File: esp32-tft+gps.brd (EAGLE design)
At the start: 34.2 x 64.8 mm, 36 parts, among them IC1 TCAN1051HGV, J4 Vertical Qwiic Connector, U2 XN04312, U8 NCP1117LPST50T3G

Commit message: actually save
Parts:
- removed -_+_G_V_T_R_E_0, -_+_G_V_T_R_E_1: MF-CON-2.54mm-01x08, SparkFun-Connectors:1X08
- removed C_SER, POW12, POW5: (no value), MF_Passives:C0603
- removed D2: BAS16, SparkFun-DiscreteSemi:SOD-323
- removed IC1: TCAN1051HGV, microbuilder:SOIC8_150MIL
- removed JP1: DB9, SparkFun-Connectors:DB9
- removed R1, R3, RCAN: (no value), 00jim:R0603
- removed U2: XN04312, SparkFun-DiscreteSemi:SOT23-6
- removed U3: (no value), SparkFun-IC-Power:TO220-IGO
- added J5: (no value), SparkFun-Connectors:1X02
- moved U$1 23.8 mm to (10.4, 25.4), turned to 0 degrees
- moved U$2 22.7 mm to (17.3, 25.4), turned to 180 degrees
- moved RCAN2 22.7 mm to (31.5, 38.6), turned to 90 degrees
- moved J2 20.8 mm to (2.03, 11.2)
- moved RCAN1 20.3 mm to (29.2, 38.6), turned to 90 degrees
- moved J1 16.8 mm to (4.06, 31.0)
- moved CEN 13.7 mm to (18.0, 31.8)
- moved R2 13.7 mm to (13.0, 36.1)
- moved R9 13.7 mm to (13.0, 31.8)
- moved REN 13.7 mm to (15.5, 31.8)
- moved RGP00 13.7 mm to (15.5, 36.1)
- moved TT1 13.7 mm to (9.40, 36.1)
- moved TT2 13.7 mm to (9.40, 31.8)
- moved J4 8.20 mm to (23.9, 39.4), turned to 180 degrees
- moved D1 5.95 mm to (12.7, 28.4)
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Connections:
- removed net CAN_H: IC1.7, JP1.1, RCAN.P$2
- removed net CAN_L: IC1.6, JP1.2, RCAN.P$1
- removed net N$4: C_SER.P$1, D2.A, R3.P$1
- removed net RAW: -_+_G_V_T_R_E_0.2, -_+_G_V_T_R_E_1.2, JP1.7, JP1.8, POW12.P$1, U3.IN
- removed net RS-IN: D2.C, JP1.5, U2.5
- removed net RS-OUT: JP1.4, R3.P$2, U2.4
- removed net UNITID: -_+_G_V_T_R_E_0.4, -_+_G_V_T_R_E_1.4, JP1.3
- net CANRX: no longer IC1.4
- net CANTX: no longer IC1.1
- net CAN_S: no longer IC1.8
- net DB9_RX: no longer U2.2
- net DB9_TX: no longer R1.P$1, U2.1
- net GND: no longer C_SER.P$2, IC1.2, U2.6
- net GND_HC: now also J5.1; no longer -_+_G_V_T_R_E_0.1, -_+_G_V_T_R_E_1.1, JP1.6, JP1.9, POW12.P$2, POW5.P$2, U3.GND
- net RX2: no longer -_+_G_V_T_R_E_0.7, -_+_G_V_T_R_E_1.8
- net RX3: no longer -_+_G_V_T_R_E_0.5, -_+_G_V_T_R_E_1.6
- net TX2: no longer -_+_G_V_T_R_E_0.8, -_+_G_V_T_R_E_1.7
- net TX3: no longer -_+_G_V_T_R_E_0.6, -_+_G_V_T_R_E_1.5
- net VCC: no longer IC1.5, R1.P$2, U2.3
- net VCC_50: now also J5.2; no longer -_+_G_V_T_R_E_0.3, -_+_G_V_T_R_E_1.3, IC1.3, POW5.P$1, U3.OUT
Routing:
- net GND_HC: track 152.7 -> 40.3 mm, vias 8 -> 3
- net UNITID: track 106.5 -> 0.00 mm, vias 1 -> 0
- net VCC_50: track 145.7 -> 43.1 mm, vias 3 -> 2
- net RAW: track 92.1 -> 0.00 mm, vias 3 -> 0
- net TX3: track 80.9 -> 0.00 mm, vias 3 -> 0
- net CAN_S: track 72.7 -> 0.00 mm, vias 2 -> 0
- net CANRX: track 69.7 -> 0.00 mm, vias 2 -> 0
- net RX2: track 63.3 -> 0.00 mm, vias 2 -> 0
- net CANTX: track 61.0 -> 0.00 mm, vias 2 -> 0
- net TX2: track 56.0 -> 0.00 mm, vias 3 -> 0
- net RX3: track 54.8 -> 0.00 mm, vias 3 -> 0
- net DB9_RX: track 54.8 -> 0.00 mm, vias 4 -> 0
- net GND: track 164.8 -> 110.7 mm, vias 7 -> 5
- net DB9_TX: track 46.0 -> 0.00 mm, vias 4 -> 0
- net RS-IN: track 30.4 -> 0.00 mm, vias 1 -> 0
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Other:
- board size 34.2 x 64.8 mm -> 34.2 x 40.9 mm

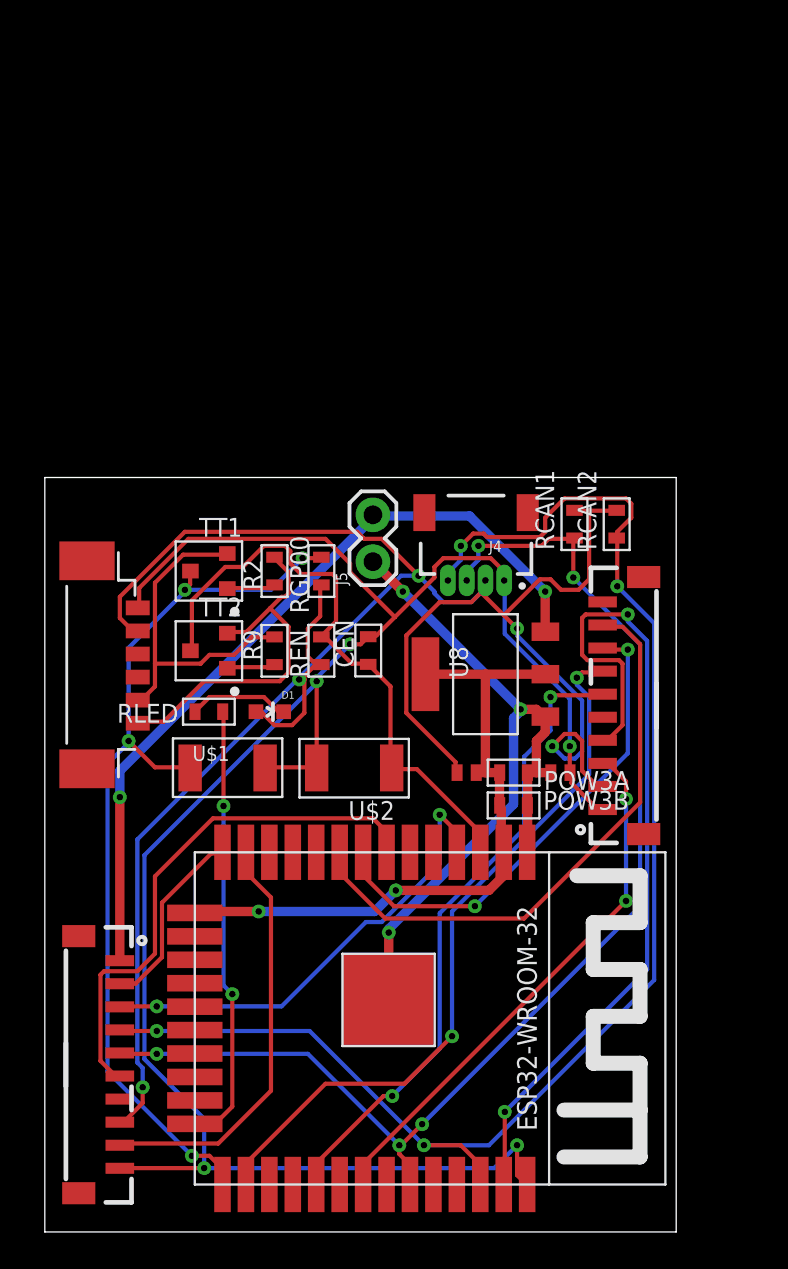
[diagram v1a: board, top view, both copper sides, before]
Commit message: Add touchscreen header directly to board
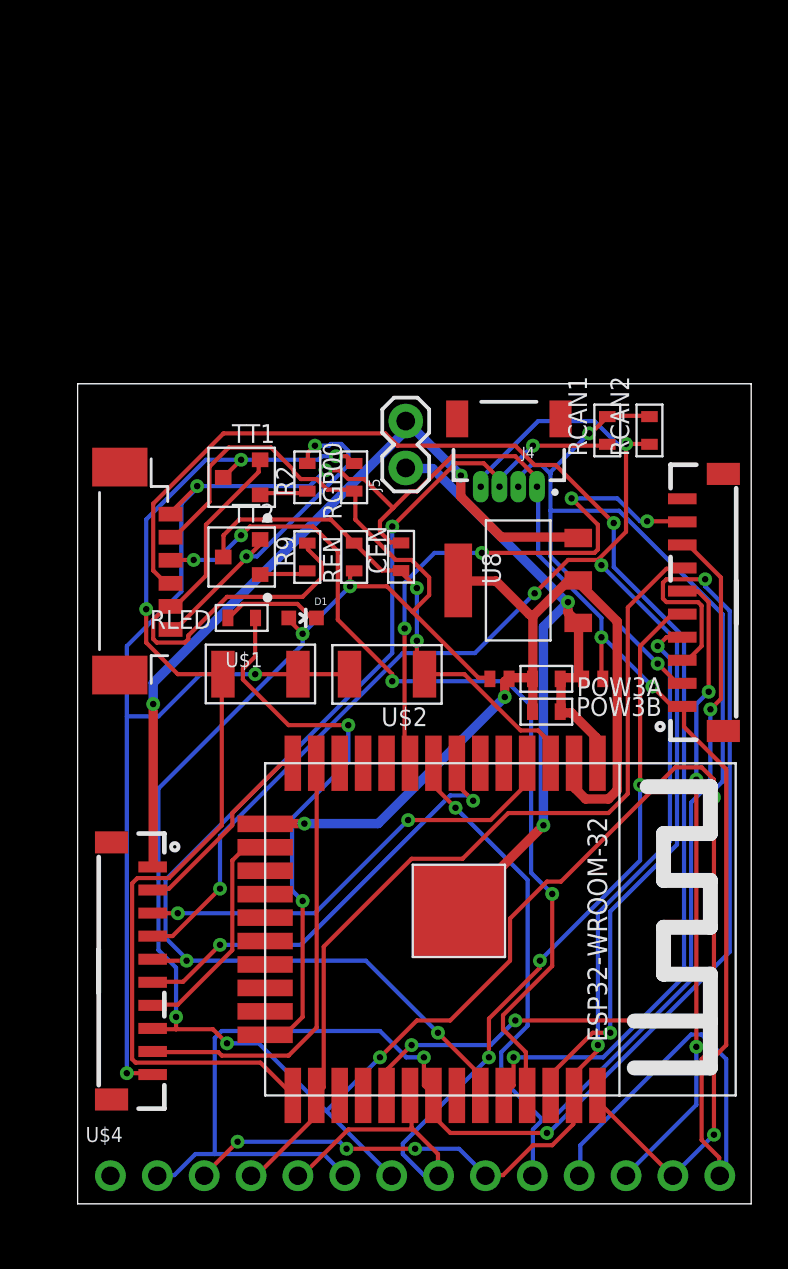
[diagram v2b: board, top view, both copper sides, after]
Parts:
- added U$4: SPI_TFT_TOUCH, 00jim:1X14_ROUND_70
- moved J3 7.06 mm to (37.6, 32.5)
- moved U$3 6.15 mm to (12.4, 25.7)
- moved RCAN2 5.38 mm to (33.3, 43.7)
- moved TT1 5.38 mm to (11.2, 41.1)
- moved J4 5.38 mm to (25.7, 44.5)
- moved R2 5.38 mm to (14.7, 41.1)
- moved RCAN1 5.38 mm to (31.0, 43.7)
- moved RGP00 5.38 mm to (17.3, 41.1)
- moved U$2 5.38 mm to (19.1, 30.5)
- moved U$1 5.38 mm to (12.2, 30.5)
- moved J2 5.38 mm to (3.81, 16.3)
- moved POW3B 5.38 mm to (27.7, 28.4)
- moved U8 5.38 mm to (26.2, 35.6)
- moved CEN 5.38 mm to (19.8, 36.8)
- moved R5 5.38 mm to (25.1, 30.2)
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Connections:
- removed net CANRX: U$3.IO16
- removed net CANTX: U$3.IO15
- removed net CAN_S: U$3.IO17
- removed net CLK: J3.5
- removed net DB9_RX: U$3.IO26
- removed net DB9_TX: U$3.IO27
- removed net RX0: J1.4
- removed net RX2: U$3.SENSOR_VN
- removed net RX3: U$3.IO34
- removed net TX0: J1.3
- removed net TX2: U$3.IO25
- removed net TX3: U$3.IO13
- net GND: now also U$4.13
- net LED: now also U$3.IO13
- net MISO: now also U$4.2, U$4.6
- net MOSI: now also U$4.3, U$4.9
- net RXI: now also J1.4
- net SCLK: now also J3.5, U$4.5, U$4.8
- net TCH_CS: now also U$4.4
- net TFT_CS: now also U$4.12
- net TFT_DC: now also U$4.10
- net TXO: now also J1.3
- net VCC: now also U$4.11, U$4.14, U$4.7
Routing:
- net VCC: track 120.2 -> 197.3 mm, vias 5 -> 8
- net RXI: track 0.00 -> 72.9 mm, vias 0 -> 2
- net MISO: track 29.4 -> 83.2 mm, vias 2 -> 3
- net SCLK: track 0.00 -> 50.6 mm, vias 0 -> 3
- net TXO: track 0.00 -> 50.0 mm, vias 0 -> 4
- net TFT_DC: track 26.8 -> 62.8 mm
- net TFT_CS: track 34.8 -> 53.9 mm, vias 2 -> 5
- net GND: track 110.7 -> 126.2 mm, vias 5 -> 7
- net LED: track 0.00 -> 12.5 mm
- net VCC_HC: track 36.3 -> 47.9 mm
- net IO00: track 50.3 -> 59.2 mm, vias 4 -> 3
- net TCH_CS: track 39.5 -> 48.1 mm, vias 2 -> 0
- net DTR: track 18.5 -> 25.4 mm
- net SCL1: track 80.0 -> 86.8 mm, vias 4 -> 5
- net MOSI: track 46.3 -> 52.6 mm, vias 2 -> 5
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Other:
- board size 34.2 x 40.9 mm -> 36.5 x 44.4 mm

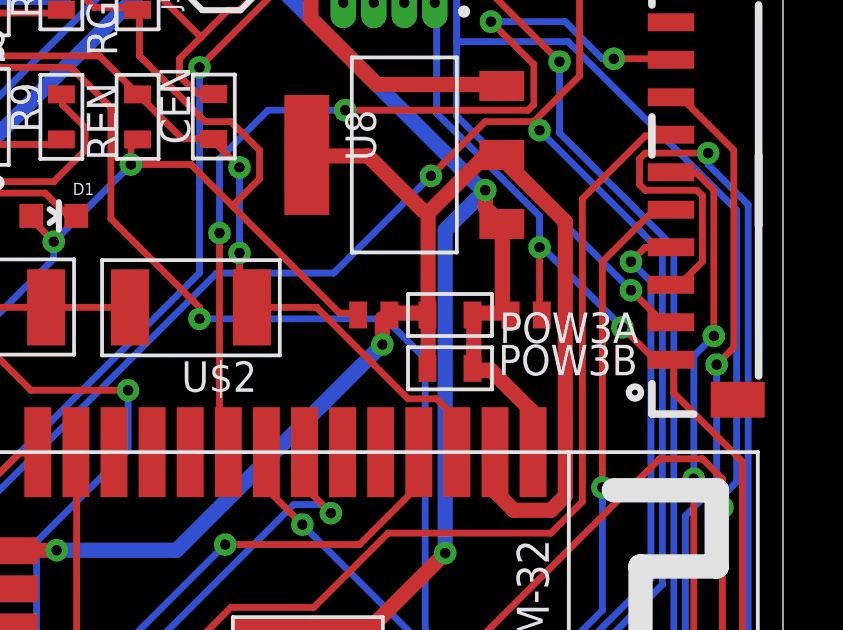
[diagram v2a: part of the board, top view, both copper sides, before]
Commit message: forgot to jumper gnd and gnd_hc
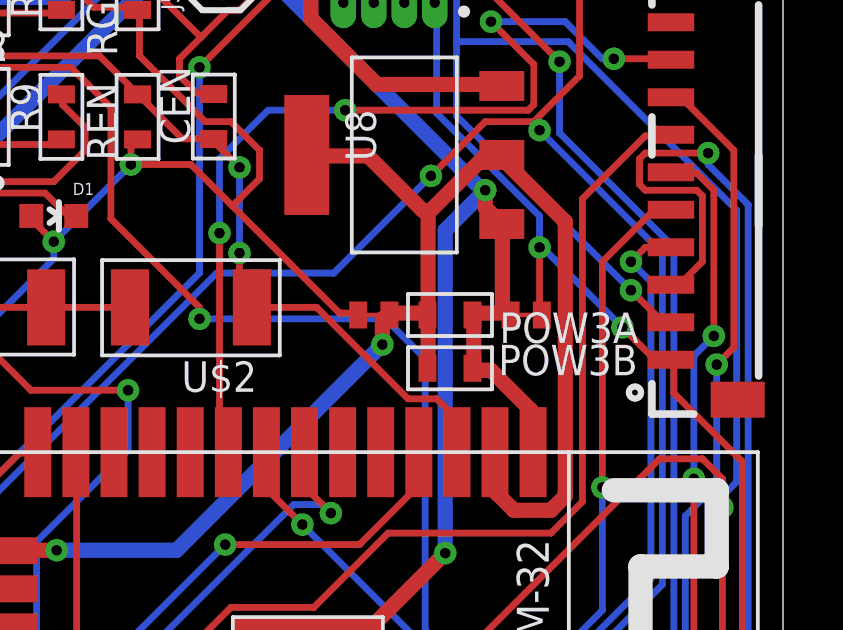
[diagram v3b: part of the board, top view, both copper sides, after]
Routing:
- net N$4: track 0.00 -> 0.51 mm
- net N$1: track 0.00 -> 0.51 mm
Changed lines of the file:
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@@
 <via x="24.5745" y="9.7155" extent="1-16" drill="0.35"/>
+</signal>
+<signal name="N$1">
+<wire x1="24.892" y1="30.226" x2="25.4" y2="30.226" width="0.1524" layer="1"/>
+</signal>
+<signal name="N$4">
+<wire x1="29.972" y1="30.226" x2="30.48" y2="30.226" width="0.1524" layer="1"/>
 </signal>
 </signals>
